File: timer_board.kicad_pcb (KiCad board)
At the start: 2 copper layers, 127 x 76.2 mm, 52 parts, among them IC1 ATMEGA32U4, P1 USBMICRO, P2 OUT_INV, P3 Trigger, P4 OUT, Q1 NPN, Q2 NPN, U1 DS3231N, U2 74HC04, Y1 RESONATORSMD

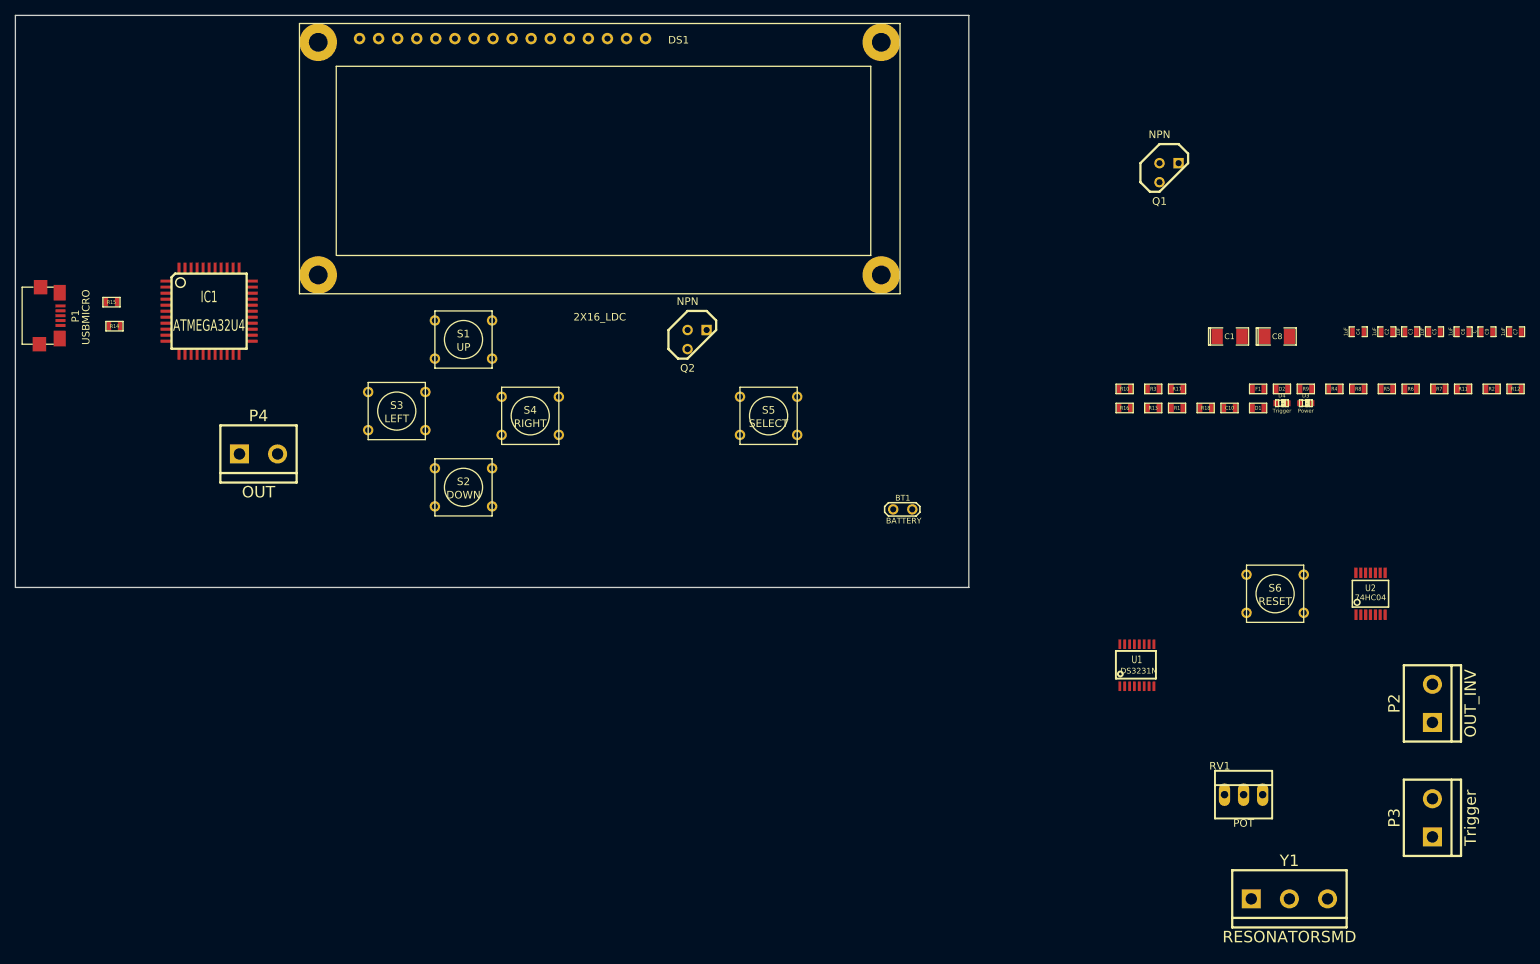
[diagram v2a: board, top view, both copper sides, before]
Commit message: Added Relay
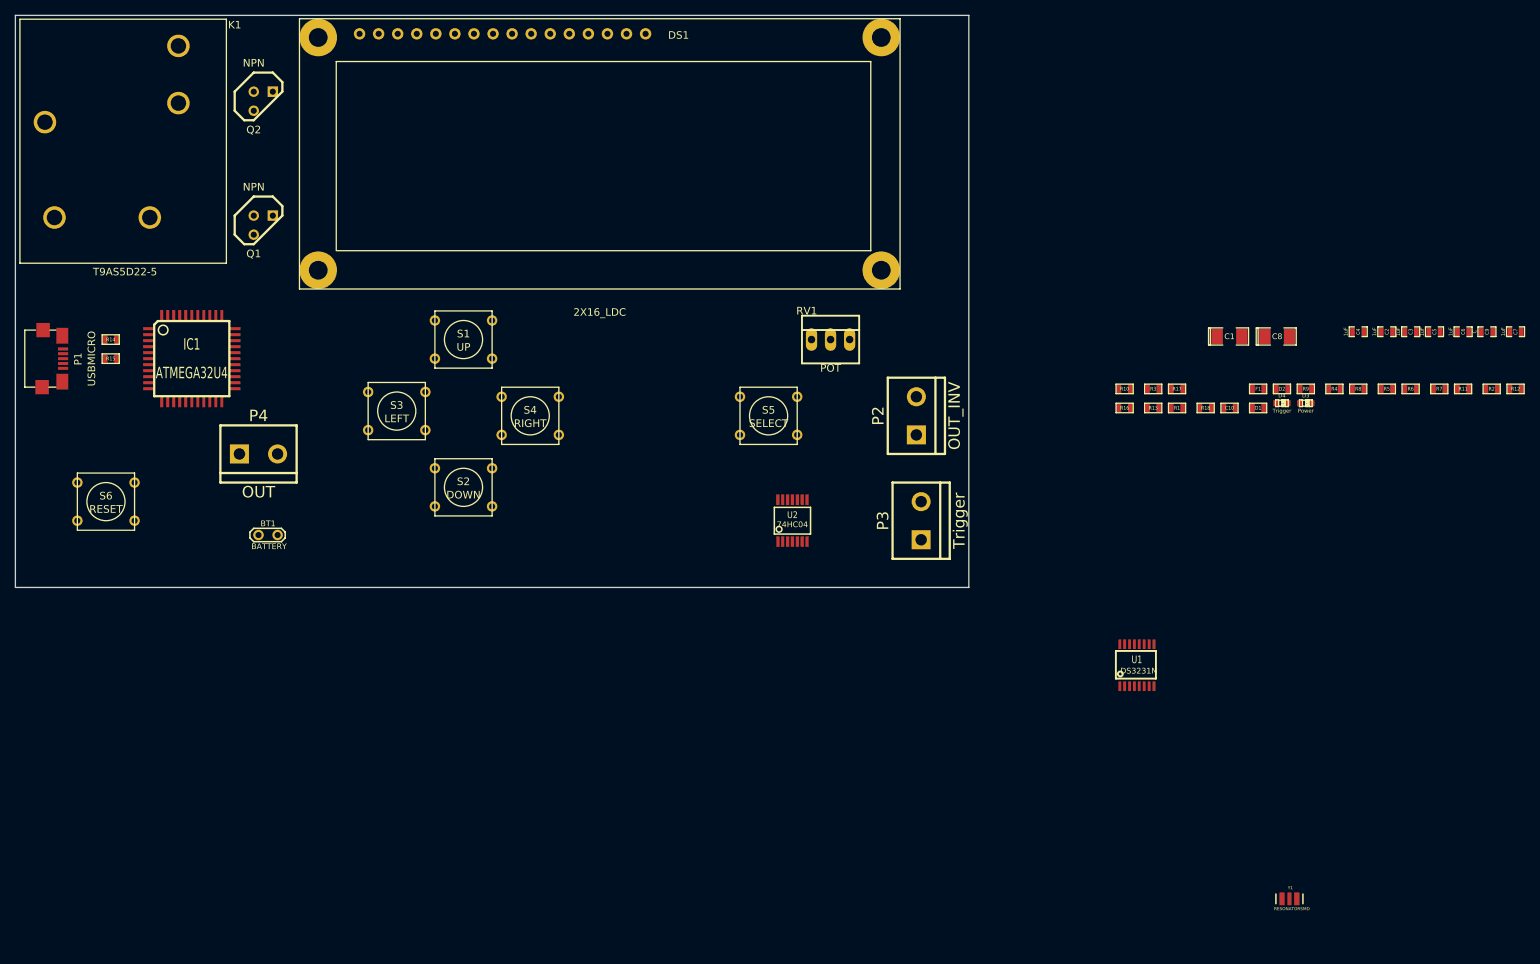
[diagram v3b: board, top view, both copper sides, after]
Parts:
- added K1: T9AS5D22-5, T9AS5D22-5, F.Cu at (40.0, 41.9)
- Y1: footprint bornier3 -> RESONATOR-SMD
- moved S6 156.2 mm to (37.5, 90.2)
- moved Q1 120.9 mm to (58.4, 53.3)
- moved BT1 84.6 mm to (59.1, 94.6)
- moved RV1 81.9 mm to (134.0, 68.6)
- moved P3 78.8 mm to (146.1, 92.7)
- moved P2 78.7 mm to (145.4, 78.7)
- moved U2 77.6 mm to (128.9, 92.7)
- moved Q2 65.9 mm to (58.4, 36.8)
- moved R15 7.52 mm to (38.1, 71.1)
- moved IC1 6.73 mm to (48.9, 71.1)
- moved P1 5.73 mm to (31.8, 71.1)
- moved R14 1.85 mm to (38.1, 68.6)
- moved DS1 0.64 mm to (78.7, 29.8)
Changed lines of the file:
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@@
 (kicad_pcb (version 3) (host pcbnew "(2013-05-16 BZR 4016)-stable")
   (general
-    (links 143)
-    (no_connects 143)
-    (area 25.349999 25.349999 127.050001 101.650001)
+    (links 145)
+    (no_connects 145)
+    (area 25.349999 25.349999 152.450001 101.650001)
     (thickness 1.6)
     (drawings 4)
     (tracks 0)
     (zones 0)
-    (modules 52)
+    (modules 53)
     (nets 49)
   )
@@
     (mod_text_size 1 1)
     (mod_text_width 0.15)
-    (pad_size 5 5)
-    (pad_drill 2.5)
+    (pad_size 3 3)
+    (pad_drill 2.06)
     (pad_to_mask_clearance 0)
     (aux_axis_origin 0 0)
@@
   )
   (module TQFP44 (layer F.Cu)
-    (at 51.2 64.8)
+    (at 48.895 71.12)
     (attr smd)
     (fp_text reference IC1 (at 0 -1.905) (layer F.SilkS)
@@
   )
   (module TO92 (layer F.Cu)
-    (at 116.205 68.58)
+    (at 58.42 36.83)
     (descr "Transistor TO92 brochage type BC237")
     (tags "TR TO92")
@@
   )
   (module TO92 (layer F.Cu)
-    (at 179.07 46.355)
+    (at 58.42 53.34)
     (descr "Transistor TO92 brochage type BC237")
     (tags "TR TO92")
@@
   )
   (module TESTPOINT (layer F.Cu)
-    (at 143.6 91.2)
+    (at 59.055 94.615)
     (descr "Connecteurs 2 pins")
     (tags "CONN DEV")
@@
   )
   (module SW_PUSH_SMALL (layer F.Cu)
-    (at 193.2 102.44)
+    (at 37.465 90.17)
     (fp_text reference S6 (at 0 -0.762) (layer F.SilkS)
       (effects (font (size 1.016 1.016) (thickness 0.2032)))
@@
   )
   (module SSOP14 (layer F.Cu)
-    (at 205.9 102.44)
+    (at 128.905 92.71)
     (attr smd)
     (fp_text reference U2 (at 0 -0.762) (layer F.SilkS)
@@
   )
   (module SM0603 (layer F.Cu)
-    (at 38.6 66.8)
+    (at 38.1 68.58)
     (attr smd)
     (fp_text reference R14 (at 0 0) (layer F.SilkS)
@@
   )
   (module SM0603 (layer F.Cu)
-    (at 38.2 63.6)
+    (at 38.1 71.12)
     (attr smd)
     (fp_text reference R15 (at 0 0) (layer F.SilkS)
@@
   )
   (module PINHEAD1-3 (layer F.Cu)
-    (at 189 129.2)
+    (at 133.985 68.58)
     (attr virtual)
     (fp_text reference RV1 (at -3.175 -3.81) (layer F.SilkS)
@@
     )
   )
-  (module bornier3 (layer F.Cu)
-    (at 195.105 143.08)
-    (descr "Bornier d'alimentation 3 pins")
-    (tags DEV)
-    (fp_text reference Y1 (at 0 -5.08) (layer F.SilkS)
-      (effects (font (size 1.524 1.524) (thickness 0.3048)))
-    )
-    (fp_text value RESONATORSMD (at 0 5.08) (layer F.SilkS)
-      (effects (font (size 1.524 1.524) (thickness 0.3048)))
-    )
-    (fp_line (start -7.62 3.81) (end -7.62 -3.81) (layer F.SilkS) (width 0.3048))
-    (fp_line (start 7.62 3.81) (end 7.62 -3.81) (layer F.SilkS) (width 0.3048))
-    (fp_line (start -7.62 2.54) (end 7.62 2.54) (layer F.SilkS) (width 0.3048))
-    (fp_line (start -7.62 -3.81) (end 7.62 -3.81) (layer F.SilkS) (width 0.3048))
-    (fp_line (start -7.62 3.81) (end 7.62 3.81) (layer F.SilkS) (width 0.3048))
-    (pad 1 thru_hole rect (at -5.08 0) (size 2.54 2.54) (drill 1.524)
-      (layers *.Cu *.Mask F.SilkS)
-      (net 19 N-000019)
-    )
-    (pad 2 thru_hole circle (at 0 0) (size 2.54 2.54) (drill 1.524)
-      (layers *.Cu *.Mask F.SilkS)
-      (net 9 GND)
-    )
-    (pad 3 thru_hole circle (at 5.08 0) (size 2.54 2.54) (drill 1.524)
-      (layers *.Cu *.Mask F.SilkS)
-      (net 18 N-000018)
-    )
-    (model device/bornier_3.wrl
-      (at (xyz 0 0 0))
-      (scale (xyz 1 1 1))
-      (rotate (xyz 0 0 0))
-    )
-  )
   (module bornier2 (layer F.Cu)
     (at 57.785 83.82)
@@
   )
   (module bornier2 (layer F.Cu)
-    (at 214.155 132.285 90)
+    (at 146.05 92.71 90)
     (descr "Bornier d'alimentation 2 pins")
     (tags DEV)
@@
   )
   (module bornier2 (layer F.Cu)
-    (at 214.155 117.045 90)
+    (at 145.415 78.74 90)
     (descr "Bornier d'alimentation 2 pins")
     (tags DEV)
@@
     )
   )
-  (module USB-MICRO-B (layer F.Cu)
-    (at 31.4 65.4 270)
-    (fp_text reference P1 (at 0.05 -2 270) (layer F.SilkS)
-      (effects (font (size 1 1) (thickness 0.15)))
-    )
-    (fp_text value USBMICRO (at 0.2 -3.4 270) (layer F.SilkS)
-      (effects (font (size 1 1) (thickness 0.15)))
-    )
-    (fp_line (start 3.8 3.75) (end 3.8 5.1) (layer F.SilkS) (width 0.15))
-    (fp_line (start 3.8 5.1) (end -3.8 5.1) (layer F.SilkS) (width 0.15))
-    (fp_line (start -3.8 5.1) (end -3.8 3.65) (layer F.SilkS) (width 0.15))
-    (fp_line (start 3.8 1.9) (end 3.8 0.95) (layer F.SilkS) (width 0.15))
-    (fp_line (start -3.8 1.75) (end -3.8 0.95) (layer F.SilkS) (width 0.15))
-    (pad 3 smd rect (at 0 0 270) (size 0.4 1.35)
-      (layers F.Cu F.Paste F.Mask)
-      (net 13 N-000004)
-    )
-    (pad 4 smd rect (at 0.65 0 270) (size 0.4 1.35)
-      (layers F.Cu F.Paste F.Mask)
-      (net 9 GND)
-    )
-    (pad 2 smd rect (at -0.65 0 270) (size 0.4 1.35)
-      (layers F.Cu F.Paste F.Mask)
-      (net 12 N-000003)
-    )
-    (pad 5 smd rect (at 1.3 0 270) (size 0.4 1.35)
-      (layers F.Cu F.Paste F.Mask)
-      (net 9 GND)
-    )
-    (pad 1 smd rect (at -1.3 0 270) (size 0.4 1.35)
-      (layers F.Cu F.Paste F.Mask)
-      (net 47 UVCC)
-    )
-    (pad "" smd rect (at -3.05 0.1 270) (size 2.1 1.6)
-      (layers F.Cu F.Paste F.Mask)
-    )
-    (pad "" smd rect (at 3.05 0.1 270) (size 2.1 1.6)
-      (layers F.Cu F.Paste F.Mask)
-    )
-    (pad "" smd rect (at 3.8 2.8 270) (size 1.9 1.8)
-      (layers F.Cu F.Paste F.Mask)
-    )
-    (pad "" smd rect (at -3.8 2.65 270) (size 1.9 1.8)
-      (layers F.Cu F.Paste F.Mask)
-    )
-  )
   (module LCD16X2 (layer F.Cu)
-    (at 78.74 30.48)
+    (at 78.74 29.845)
     (fp_text reference DS1 (at 35 -1.8) (layer F.SilkS)
       (effects (font (size 1 1) (thickness 0.15)))
@@
     )
   )
+  (module T9AS5D22-5 (layer F.Cu)
+    (at 40.005 41.91)
+    (fp_text reference K1 (at 14.605 -15.24) (layer F.SilkS)
+      (effects (font (size 1 1) (thickness 0.15)))
+    )
+    (fp_text value T9AS5D22-5 (at 0 17.653) (layer F.SilkS)
+      (effects (font (size 1 1) (thickness 0.15)))
+    )
+    (fp_line (start -14 -16) (end 13.5 -16) (layer F.SilkS) (width 0.15))
+    (fp_line (start 13.5 -16) (end 13.5 16.5) (layer F.SilkS) (width 0.15))
+    (fp_line (start 13.5 16.5) (end -14 16.5) (layer F.SilkS) (width 0.15))
+    (fp_line (start -14 16.5) (end -14 -16) (layer F.SilkS) (width 0.15))
+    (pad 5 thru_hole circle (at 7.112 -12.446) (size 3 3) (drill 2.06)
+      (layers *.Cu *.Mask F.SilkS)
+    )
+    (pad 4 thru_hole circle (at 7.112 -4.826) (size 3 3) (drill 2.06)
+      (layers *.Cu *.Mask F.SilkS)
+    )
+    (pad 1 thru_hole circle (at -10.668 -2.286) (size 3 3) (drill 2.06)
+      (layers *.Cu *.Mask F.SilkS)
+    )
+    (pad 3 thru_hole circle (at 3.302 10.414) (size 3 3) (drill 2.06)
+      (layers *.Cu *.Mask F.SilkS)
+      (net 17 N-000016)
+    )
+    (pad 2 thru_hole circle (at -9.398 10.414) (size 3 3) (drill 2.06)
+      (layers *.Cu *.Mask F.SilkS)
+      (net 1 +5V)
+    )
+  )
+  (module RESONATOR-SMD (layer F.Cu)
+    (at 195.105 143.08)
+    (attr smd)
+    (fp_text reference Y1 (at 0.127 -1.4732) (layer F.SilkS)
+      (effects (font (size 0.4064 0.4064) (thickness 0.0889)))
+    )
+    (fp_text value RESONATORSMD (at 0.3302 1.3208) (layer F.SilkS)
+      (effects (font (size 0.4064 0.4064) (thickness 0.0889)))
+    )
+    (fp_line (start 1.79832 -0.6477) (end 1.79832 0.6477) (layer F.SilkS) (width 0.2032))
+    (fp_line (start -1.79832 0.6477) (end -1.79832 -0.6477) (layer F.SilkS) (width 0.2032))
+    (pad 1 smd rect (at -0.9906 0) (size 0.6985 1.69926)
+      (layers F.Cu F.Paste F.Mask)
+      (net 19 N-000019)
+    )
+    (pad 2 smd rect (at 0 0) (size 0.5461 1.69926)
+      (layers F.Cu F.Paste F.Mask)
+      (net 9 GND)
+    )
+    (pad 3 smd rect (at 0.9906 0) (size 0.6985 1.69926)
+      (layers F.Cu F.Paste F.Mask)
+      (net 18 N-000018)
+    )
+  )
+  (module USB-MICRO-B (layer F.Cu)
+    (at 31.75 71.12 270)
+    (fp_text reference P1 (at 0.05 -2 270) (layer F.SilkS)
+      (effects (font (size 1 1) (thickness 0.15)))
+    )
+    (fp_text value USBMICRO (at 0 -3.81 270) (layer F.SilkS)
+      (effects (font (size 1 1) (thickness 0.15)))
+    )
+    (fp_line (start 3.8 3.75) (end 3.8 5.1) (layer F.SilkS) (width 0.15))
+    (fp_line (start 3.8 5.1) (end -3.8 5.1) (layer F.SilkS) (width 0.15))
+    (fp_line (start -3.8 5.1) (end -3.8 3.65) (layer F.SilkS) (width 0.15))
+    (fp_line (start 3.8 1.9) (end 3.8 0.95) (layer F.SilkS) (width 0.15))
+    (fp_line (start -3.8 1.75) (end -3.8 0.95) (layer F.SilkS) (width 0.15))
+    (pad 3 smd rect (at 0 0 270) (size 0.4 1.35)
+      (layers F.Cu F.Paste F.Mask)
+      (net 13 N-000004)
+    )
+    (pad 4 smd rect (at 0.65 0 270) (size 0.4 1.35)
+      (layers F.Cu F.Paste F.Mask)
+      (net 9 GND)
+    )
+    (pad 2 smd rect (at -0.65 0 270) (size 0.4 1.35)
+      (layers F.Cu F.Paste F.Mask)
+      (net 12 N-000003)
+    )
+    (pad 5 smd rect (at 1.3 0 270) (size 0.4 1.35)
+      (layers F.Cu F.Paste F.Mask)
+      (net 9 GND)
+    )
+    (pad 1 smd rect (at -1.3 0 270) (size 0.4 1.35)
+      (layers F.Cu F.Paste F.Mask)
+      (net 47 UVCC)
+    )
+    (pad "" smd rect (at -3.05 0.1 270) (size 2.1 1.6)
+      (layers F.Cu F.Paste F.Mask)
+    )
+    (pad "" smd rect (at 3.05 0.1 270) (size 2.1 1.6)
+      (layers F.Cu F.Paste F.Mask)
+    )
+    (pad "" smd rect (at 3.8 2.8 270) (size 1.9 1.8)
+      (layers F.Cu F.Paste F.Mask)
+    )
+    (pad "" smd rect (at -3.8 2.65 270) (size 1.9 1.8)
+      (layers F.Cu F.Paste F.Mask)
+    )
+  )
